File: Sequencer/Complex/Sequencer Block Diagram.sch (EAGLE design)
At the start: 1 part, among them IC1 74386N

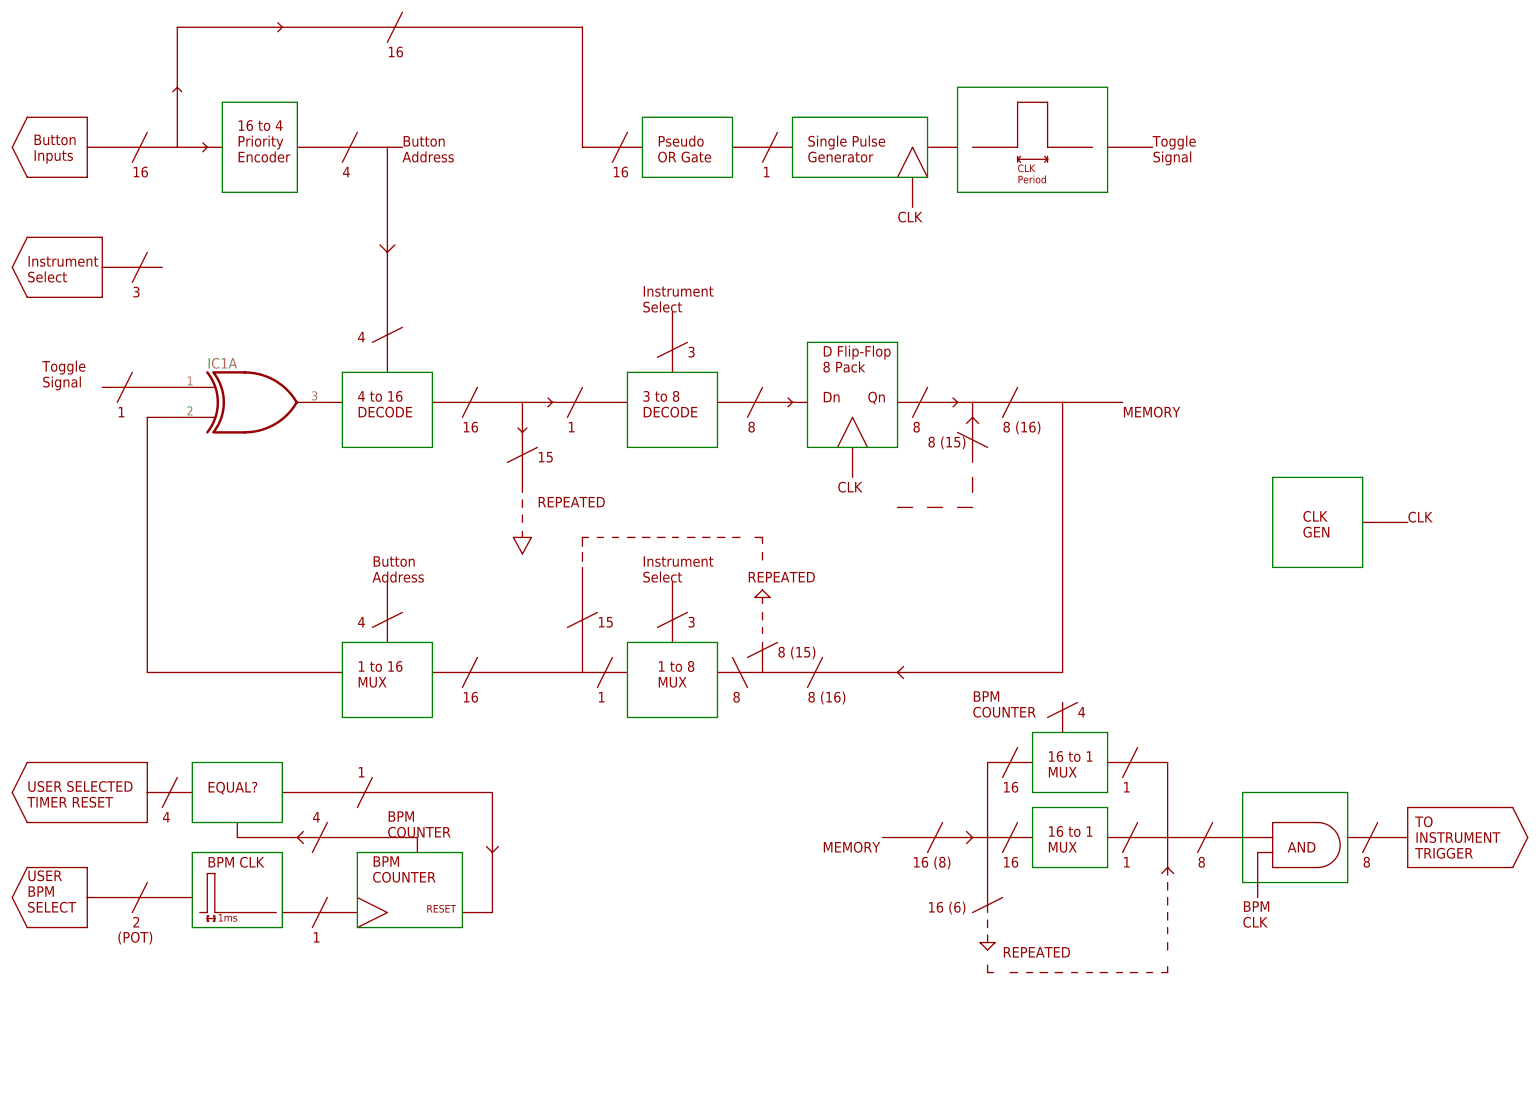
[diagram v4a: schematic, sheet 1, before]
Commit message: Updated sequencer diagram
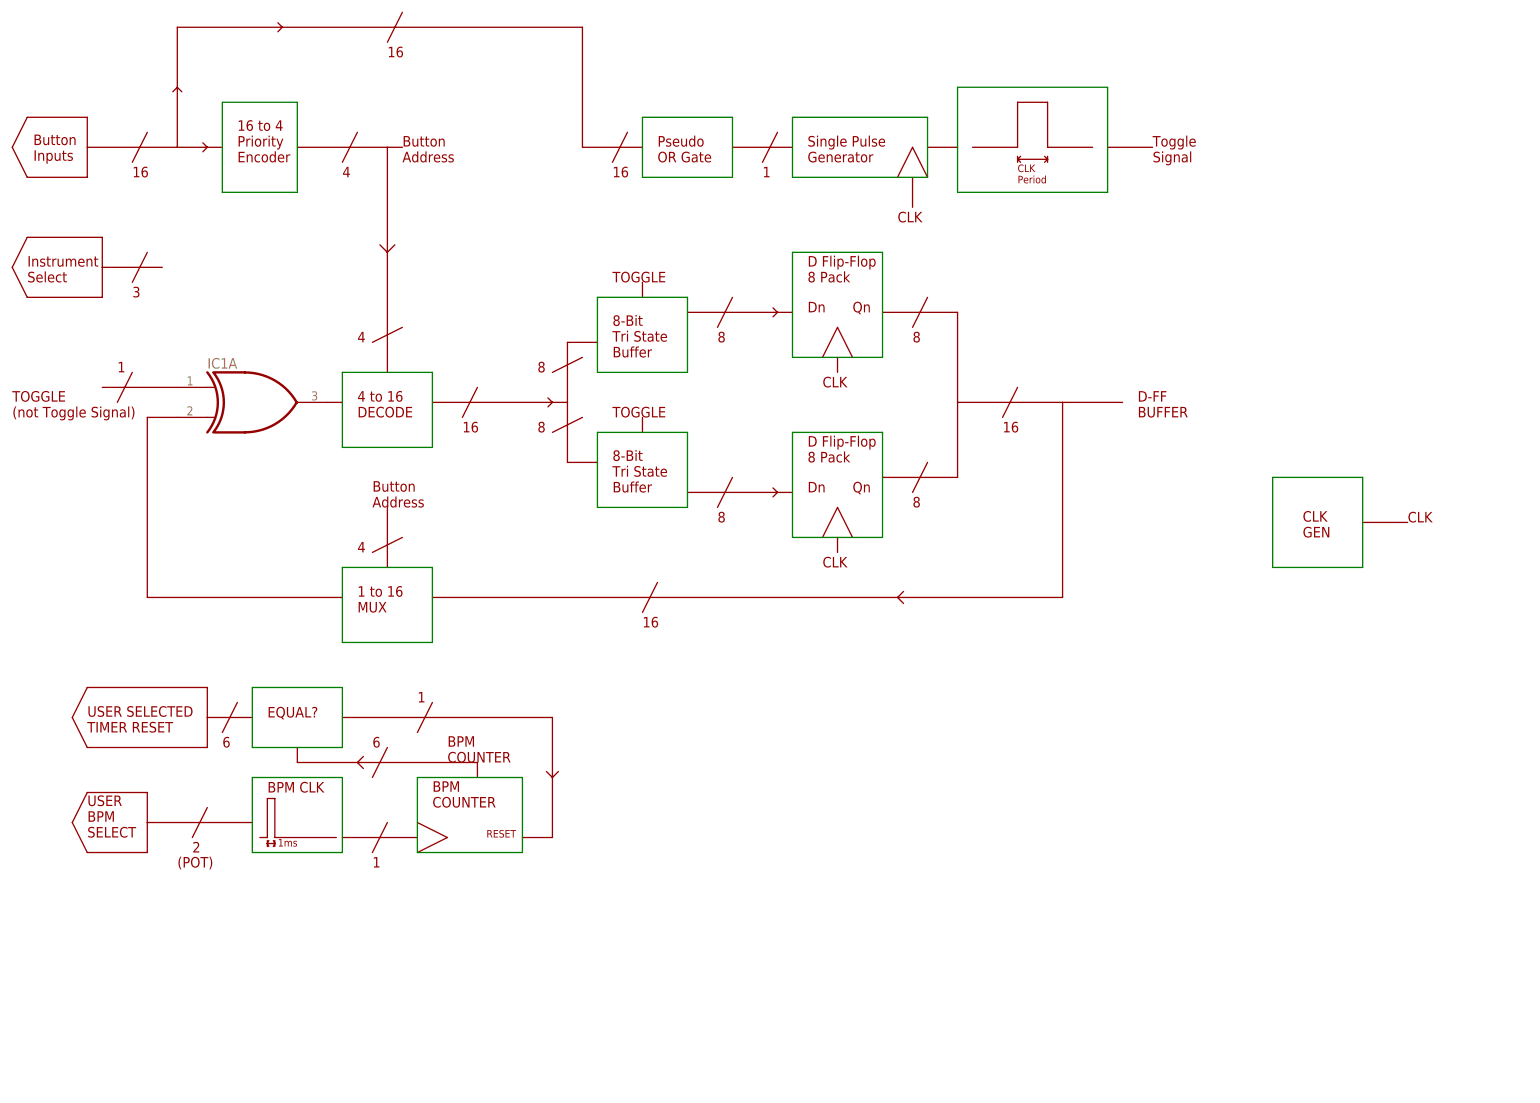
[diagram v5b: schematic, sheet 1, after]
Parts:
- added R1: 1k, rcl:R-US_0204/5
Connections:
- new net GND: R1.1
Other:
- note added: "(EN1)'(EN0)'LOAD"
- note added: "(EN1)'(EN0)'READ"
- note added: "(EN1)'(EN0)LOAD"
- note added: "(EN1)(EN0)'READ"
- note added: "0V"
- note added: "8-Bit Counter"
- note added: "8-Bit Tri State BUFFER"
- note added: "8-Bit Tri State Buffer"
- note added: "D-FF BUFFER"
- note added: "D-FF IN (0)"
- note added: "D-FF IN (1)"
- note added: "DATA BUS (8)"
- note added: "EN0"
- note added: "EN1"
- note added: "LOAD"
- note added: "Measure Select"
- note added: "Reading From RAM into Buffer"
- note added: "TOGGLE"
- note added: "TOGGLE (not Toggle Signal)"
- note removed: "1 to 8 MUX"
- note removed: "15"
- note removed: "16 (6)"
- note removed: "16 (8)"
- note removed: "16 to 1 MUX"
- note removed: "3 to 8 DECODE"
- note removed: "8 (15)"
- note removed: "8 (16)"
- note removed: "AND"
- note removed: "Loading From RAM into Buffer"
- note removed: "MEMORY"
- note removed: "REPEATED"
- note removed: "TO INSTRUMENT TRIGGER"

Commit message: finishing touches
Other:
- note added: "TO BUTTON LEDS"
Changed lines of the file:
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@@
 <wire x1="25.4" y1="165.1" x2="35.56" y2="165.1" width="0.1524" layer="94"/>
 <wire x1="33.02" y1="167.64" x2="30.48" y2="162.56" width="0.1524" layer="94"/>
-<text x="30.48" y="160.02" size="1.778" layer="94">3</text>
+<text x="30.48" y="160.02" size="1.778" layer="94">4</text>
 <wire x1="160.02" y1="109.22" x2="161.036" y2="110.236" width="0.1524" layer="94"/>
 <wire x1="160.02" y1="109.22" x2="161.036" y2="108.204" width="0.1524" layer="94"/>
@@
 <text x="129.54" y="152.4" size="1.778" layer="94">8</text>
 <text x="129.54" y="121.92" size="1.778" layer="94">8</text>
+<wire x1="187.96" y1="142.24" x2="187.96" y2="154.94" width="0.1524" layer="94"/>
+<wire x1="187.96" y1="154.94" x2="215.9" y2="154.94" width="0.1524" layer="94"/>
+<text x="218.44" y="152.4" size="1.778" layer="94">TO BUTTON
+LEDS</text>
+<wire x1="215.9" y1="160.02" x2="215.9" y2="149.86" width="0.1524" layer="94"/>
+<wire x1="215.9" y1="149.86" x2="233.68" y2="149.86" width="0.1524" layer="94"/>
+<wire x1="233.68" y1="149.86" x2="236.22" y2="154.94" width="0.1524" layer="94"/>
+<wire x1="236.22" y1="154.94" x2="233.68" y2="160.02" width="0.1524" layer="94"/>
+<wire x1="215.9" y1="160.02" x2="233.68" y2="160.02" width="0.1524" layer="94"/>
 </plain>
 <instances>

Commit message: K I think this is done
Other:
- note added: "BPM CLK Pulse"
- note added: "BUTTON INPUT BUFFER"
- note added: "Measure"
- note added: "OR"
- note added: "Single Pulse Gen"
- note added: "Switched Instrument Signal"
- note added: "XOR"
- note added: "div 128"

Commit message: k this should be good now
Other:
- note added: "READ"
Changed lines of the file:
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@@
 BUFFER</text>
 <wire x1="170.18" y1="99.06" x2="170.18" y2="101.6" width="0.1524" layer="94"/>
-<text x="166.878" y="101.854" size="1.778" layer="94">LOAD</text>
 <text x="40.64" y="91.44" size="1.778" layer="94">D-FF
 IN (0)</text>
@@
 <text x="40.64" y="71.12" size="1.778" layer="94">D-FF
 IN (1)</text>
+<text x="167.64" y="101.6" size="1.778" layer="94">READ</text>
 </plain>
 <instances>
